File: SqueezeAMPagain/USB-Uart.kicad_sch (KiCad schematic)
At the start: 12 parts, among them J5 USB_B_Micro, J9 Conn_01x06_Pin, Q4 Q_NPN_BEC, Q5 Q_NPN_BEC, U3 CP2102N-Axx-xQFN28

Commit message: Update SqueezeAMPagain.kicad_pcb, SqueezeAMPagain.kicad_prl, USB-Uart.kicad_sch, and 4 more files
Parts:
- removed L10: 680nH, Inductor_SMD:L_0805_2012Metric, symbol Device:L
- added C76, C77, C80: 100n, Capacitor_SMD:C_0603_1608Metric, symbol Device:C
- added C78, C79: 2.2u/25V, Capacitor_SMD:C_0805_2012Metric, symbol Device:C
- added FB6: 600Ω@100MHz 500mA, Inductor_SMD:L_0805_2012Metric, symbol Device:FerriteBead_Small
- added R29, R30, R31: 10k, Resistor_SMD:R_0603_1608Metric, symbol Device:R
- added U7: AMS1117-3.3, Package_TO_SOT_SMD:SOT-223-3_TabPin2, symbol Regulator_Linear:AMS1117-3.3
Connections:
- net +3.3V: now also C76.1, U7.2 (VO)
- net GND: now also C76.2, C77.2, C78.2, R31.1, U7.1 (GND)
- net V_{USB}: now also U3.7 (VREGIN), C77.1, C78.1, FB6.2, R29.1, R30.1, U7.3 (VI); no longer U3.8 (VBUS)
- net at D1.1 (K): now also FB6.1
- net at U3.6 (VDD): now also C79.1, C80.1
- new net: R29.2, R30.2, R31.2, U3.8 (VBUS)
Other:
- note added: "max Output of internal regulator?"
- moved on the sheet: C46, C47

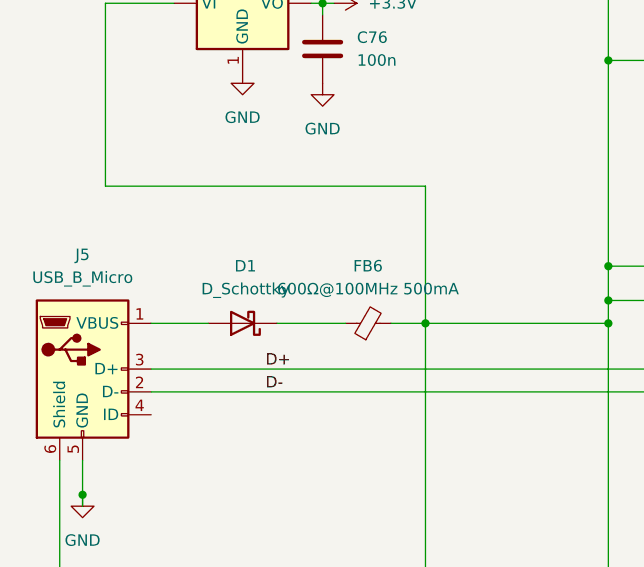
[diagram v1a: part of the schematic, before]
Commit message: Update SqueezeAMPagain.kicad_pcb, SqueezeAMPagain.kicad_sch, USB-Uart.kicad_sch, and 4 more files
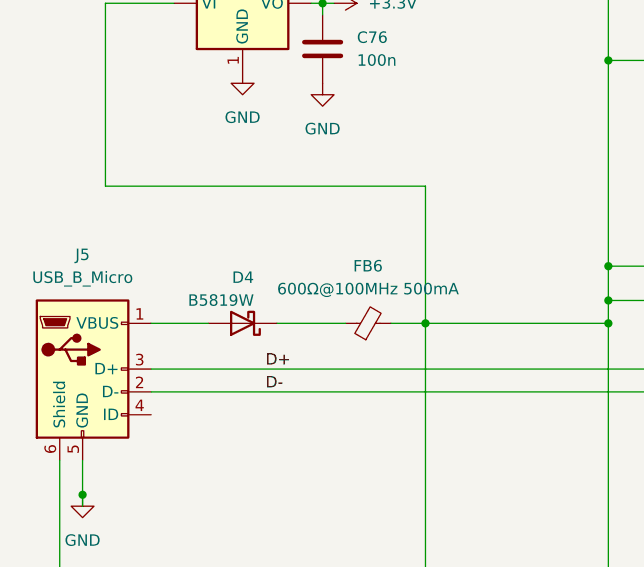
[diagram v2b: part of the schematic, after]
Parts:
- removed D1: D_Schottky, Diode_SMD:D_0603_1608Metric, symbol Device:D_Schottky
- added D4: B5819W, Diode_SMD:D_SOD-123, symbol Device:D_Schottky
- R29, R30, R31: JLCPCB# (none) -> C25804
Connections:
- net at FB6.1: now also D4.1 (K)
- net at J5.1 (VBUS): now also D4.2 (A)
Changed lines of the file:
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@@
+	)
+	(symbol
+		(lib_id "Device:C")
+		(at 80.01 116.84 0)
+		(unit 1)
+		(exclude_from_sim no)
+		(in_bom yes)
+		(on_board yes)
+		(dnp no)
+		(fields_autoplaced yes)
+		(property "Reference" "C47"
+			(at 83.82 115.5699 0)
+			(effects
+				(font
+					(size 1.27 1.27)
+				)
+				(justify left)
+			)
+		)
+		(property "Value" "2.2u/25V"
+			(at 83.82 118.1099 0)
+			(effects
+				(font
+					(size 1.27 1.27)
+				)
+				(justify left)
+			)
+		)
+		(property "Footprint" "Capacitor_SMD:C_0805_2012Metric"
+			(at 80.9752 120.65 0)
+			(effects
+				(font
+					(size 1.27 1.27)
+				)
+				(hide yes)
+			)
+		)
+		(property "Datasheet" "~"
+			(at 80.01 116.84 0)
+			(effects
+				(font
+					(size 1.27 1.27)
+				)
+				(hide yes)
+			)
+		)
+		(property "Description" "Unpolarized capacitor"
+			(at 80.01 116.84 0)
+			(effects
+				(font
+					(size 1.27 1.27)
+				)
+				(hide yes)
+			)
+		)
+		(pin "2"
+		)
+		(pin "1"
+		)
+		(instances
+			(project "SqueezeAMPagain"
+				(path "/3675160b-d9e5-490e-b506-2a7966e79ed0/86167bdd-1d24-4489-95f0-02f70a80611f"
+					(reference "C47")
+					(unit 1)
+				)
+			)
+		)
+	)
+	(symbol
+		(lib_id "Device:Q_NPN_BEC")
+		(at 189.23 85.09 0)
+		(unit 1)
+		(exclude_from_sim no)
+		(in_bom yes)
+		(on_board yes)
+		(dnp no)
+		(fields_autoplaced yes)
+		(property "Reference" "Q4"
+			(at 194.31 83.8199 0)
+			(effects
+				(font
+					(size 1.27 1.27)
+				)
+				(justify left)
+			)
+		)
+		(property "Value" "Q_NPN_BEC"
+			(at 194.31 86.3599 0)
+			(effects
+				(font
+					(size 1.27 1.27)
+				)
+				(justify left)
+			)
+		)
+		(property "Footprint" "Package_TO_SOT_SMD:SOT-23"
+			(at 194.31 82.55 0)
+			(effects
+				(font
+					(size 1.27 1.27)
+				)
+				(hide yes)
+			)
+		)
+		(property "Datasheet" "~"
+			(at 189.23 85.09 0)
+			(effects
+				(font
+					(size 1.27 1.27)
+				)
+				(hide yes)
+			)
+		)
+		(property "Description" "NPN transistor, base/emitter/collector"
+			(at 189.23 85.09 0)
+			(effects
+				(font
+					(size 1.27 1.27)
+				)
+				(hide yes)
+			)
+		)
+		(pin "3"
+		)
+		(pin "2"
+		)
+		(pin "1"
+		)
+		(instances
+			(project "SqueezeAMPagain"
+				(path "/3675160b-d9e5-490e-b506-2a7966e79ed0/86167bdd-1d24-4489-95f0-02f70a80611f"
+					(reference "Q4")
+					(unit 1)
+				)
+			)
+		)
 	)
 	(symbol
@@
 		(on_board yes)
 		(dnp no)
-		(fields_autoplaced yes)
-		(property "Reference" "D1"
-			(at 39.6875 62.23 0)
-			(effects
-				(font
-					(size 1.27 1.27)
-				)
-			)
-		)
-		(property "Value" "D_Schottky"
-			(at 39.6875 64.77 0)
-			(effects
-				(font
-					(size 1.27 1.27)
-				)
-			)
-		)
-		(property "Footprint" "Diode_SMD:D_0603_1608Metric"
+		(property "Reference" "D4"
+			(at 40.64 63.5 0)
+			(effects
+				(font
+					(size 1.27 1.27)
+				)
+				(justify left)
+			)
+		)
+		(property "Value" "B5819W"
+			(at 40.64 66.04 0)
+			(effects
+				(font
+					(size 1.27 1.27)
+				)
+				(justify left)
+			)
+		)
+		(property "Footprint" "Diode_SMD:D_SOD-123"
 			(at 39.37 68.58 0)
 			(effects
@@
 			)
 		)
+		(property "JLCPCB#" "C8598"
+			(at 39.37 68.58 90)
+			(effects
+				(font
+					(size 1.27 1.27)
+				)
+				(hide yes)
+			)
+		)
+		(pin "1"
+		)
 		(pin "2"
 		)
-		(pin "1"
-		)
-		(instances
-			(project ""
-				(path "/3675160b-d9e5-490e-b506-2a7966e79ed0/86167bdd-1d24-4489-95f0-02f70a80611f"
-					(reference "D1")
-					(unit 1)
-				)
-			)
-		)
-	)
-	(symbol
-		(lib_id "Device:C")
-		(at 80.01 116.84 0)
-		(unit 1)
-		(exclude_from_sim no)
-		(in_bom yes)
-		(on_board yes)
-		(dnp no)
-		(fields_autoplaced yes)
-		(property "Reference" "C47"
-			(at 83.82 115.5699 0)
-			(effects
-				(font
-					(size 1.27 1.27)
-				)
-				(justify left)
-			)
-		)
-		(property "Value" "2.2u/25V"
-			(at 83.82 118.1099 0)
-			(effects
-				(font
-					(size 1.27 1.27)
-				)
-				(justify left)
-			)
-		)
-		(property "Footprint" "Capacitor_SMD:C_0805_2012Metric"
-			(at 80.9752 120.65 0)
-			(effects
-				(font
-					(size 1.27 1.27)
-				)
-				(hide yes)
-			)
-		)
-		(property "Datasheet" "~"
-			(at 80.01 116.84 0)
-			(effects
-				(font
-					(size 1.27 1.27)
-				)
-				(hide yes)
-			)
-		)
-		(property "Description" "Unpolarized capacitor"
-			(at 80.01 116.84 0)
-			(effects
-				(font
-					(size 1.27 1.27)
-				)
-				(hide yes)
-			)
-		)
-		(pin "2"
-		)
-		(pin "1"
-		)
-		(instances
-			(project "SqueezeAMPagain"
-				(path "/3675160b-d9e5-490e-b506-2a7966e79ed0/86167bdd-1d24-4489-95f0-02f70a80611f"
-					(reference "C47")
-					(unit 1)
-				)
-			)
-		)
-	)
-	(symbol
-		(lib_id "Device:Q_NPN_BEC")
-		(at 189.23 85.09 0)
-		(unit 1)
-		(exclude_from_sim no)
-		(in_bom yes)
-		(on_board yes)
-		(dnp no)
-		(fields_autoplaced yes)
-		(property "Reference" "Q4"
-			(at 194.31 83.8199 0)
-			(effects
-				(font
-					(size 1.27 1.27)
-				)
-				(justify left)
-			)
-		)
-		(property "Value" "Q_NPN_BEC"
-			(at 194.31 86.3599 0)
-			(effects
-				(font
-					(size 1.27 1.27)
-				)
-				(justify left)
-			)
-		)
-		(property "Footprint" "Package_TO_SOT_SMD:SOT-23"
-			(at 194.31 82.55 0)
-			(effects
-				(font
-					(size 1.27 1.27)
-				)
-				(hide yes)
-			)
-		)
-		(property "Datasheet" "~"
-			(at 189.23 85.09 0)
-			(effects
-				(font
-					(size 1.27 1.27)
-				)
-				(hide yes)
-			)
-		)
-		(property "Description" "NPN transistor, base/emitter/collector"
-			(at 189.23 85.09 0)
-			(effects
-				(font
-					(size 1.27 1.27)
-				)
-				(hide yes)
-			)
-		)
-		(pin "3"
-		)
-		(pin "2"
-		)
-		(pin "1"
-		)
-		(instances
-			(project "SqueezeAMPagain"
-				(path "/3675160b-d9e5-490e-b506-2a7966e79ed0/86167bdd-1d24-4489-95f0-02f70a80611f"
-					(reference "Q4")
+		(instances
+			(project "SqueezeAMPagain"
+				(path "/3675160b-d9e5-490e-b506-2a7966e79ed0/86167bdd-1d24-4489-95f0-02f70a80611f"
+					(reference "D4")
 					(unit 1)
 				)
@@
 			)
 		)
+		(property "JLCPCB#" "C25804"
+			(at 90.17 62.23 0)
+			(effects
+				(font
+					(size 1.27 1.27)
+				)
+				(hide yes)
+			)
+		)
 		(pin "1"
 		)
@@
 		)
 		(property "Description" "Resistor"
+			(at 90.17 66.04 0)
+			(effects
+				(font
+					(size 1.27 1.27)
+				)
+				(hide yes)
+			)
+		)
+		(property "JLCPCB#" "C25804"
 			(at 90.17 66.04 0)
 			(effects
@@
 			(at 101.6 87.63 0)
 			(effects
+				(font
+					(size 1.27 1.27)
+				)
+				(hide yes)
+			)
+		)
+		(property "JLCPCB#" "C25804"
+			(at 101.6 87.63 0)
+			(effects

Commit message: Update SqueezeAMPagain.kicad_pcb, SqueezeAMPagain.kicad_prl, SqueezeAMPagain.kicad_pro, and 6 more files
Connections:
- net GND: now also C79.2, C80.2
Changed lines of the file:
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@@
+	)
+	(symbol
+		(lib_id "power:GND")
+		(at 134.62 49.53 0)
+		(unit 1)
+		(exclude_from_sim no)
+		(in_bom yes)
+		(on_board yes)
+		(dnp no)
+		(fields_autoplaced yes)
+		(property "Reference" "#PWR0109"
+			(at 134.62 55.88 0)
+			(effects
+				(font
+					(size 1.27 1.27)
+				)
+				(hide yes)
+			)
+		)
+		(property "Value" "GND"
+			(at 134.62 54.61 0)
+			(effects
+				(font
+					(size 1.27 1.27)
+				)
+			)
+		)
+		(property "Footprint" ""
+			(at 134.62 49.53 0)
+			(effects
+				(font
+					(size 1.27 1.27)
+				)
+				(hide yes)
+			)
+		)
+		(property "Datasheet" ""
+			(at 134.62 49.53 0)
+			(effects
+				(font
+					(size 1.27 1.27)
+				)
+				(hide yes)
+			)
+		)
+		(property "Description" "Power symbol creates a global label with name \"GND\" , ground"
+			(at 134.62 49.53 0)
+			(effects
+				(font
+					(size 1.27 1.27)
+				)
+				(hide yes)
+			)
+		)
+		(pin "1"
+		)
+		(instances
+			(project "SqueezeAMPagain"
+				(path "/3675160b-d9e5-490e-b506-2a7966e79ed0/86167bdd-1d24-4489-95f0-02f70a80611f"
+					(reference "#PWR0109")
+					(unit 1)
+				)
+			)
+		)
 	)
 	(symbol
@@
 					(unit 1)
 				)
+			)
+		)
+	)
+	(symbol
+		(lib_id "power:GND")
+		(at 147.32 49.53 0)
+		(unit 1)
+		(exclude_from_sim no)
+		(in_bom yes)
+		(on_board yes)
+		(dnp no)
+		(fields_autoplaced yes)
+		(property "Reference" "#PWR0110"
+			(at 147.32 55.88 0)
+			(effects
+				(font
+					(size 1.27 1.27)
+				)
+				(hide yes)
+			)
+		)
+		(property "Value" "GND"
+			(at 147.32 54.61 0)
+			(effects
+				(font
+					(size 1.27 1.27)
+				)
+			)
+		)
+		(property "Footprint" ""
+			(at 147.32 49.53 0)
+			(effects
+				(font
+					(size 1.27 1.27)
+				)
+				(hide yes)
+			)
+		)
+		(property "Datasheet" ""
+			(at 147.32 49.53 0)
+			(effects
+				(font
+					(size 1.27 1.27)
+				)
+				(hide yes)
+			)
+		)
+		(property "Description" "Power symbol creates a global label with name \"GND\" , ground"
+			(at 147.32 49.53 0)
+			(effects
+				(font
+					(size 1.27 1.27)
+				)
+				(hide yes)
+			)
+		)
+		(pin "1"
+		)
+		(instances
+			(project "SqueezeAMPagain"
+				(path "/3675160b-d9e5-490e-b506-2a7966e79ed0/86167bdd-1d24-4489-95f0-02f70a80611f"
+					(reference "#PWR0110")
+					(unit 1)
+				)

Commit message: Update SqueezeAMPagain.kicad_pcb, SqueezeAMPagain.kicad_prl, SqueezeAMPagain.kicad_pro, and 7 more files
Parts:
- removed C76: 100n, Capacitor_SMD:C_0603_1608Metric, symbol Device:C
- removed U7: AMS1117-3.3, Package_TO_SOT_SMD:SOT-223-3_TabPin2, symbol Regulator_Linear:AMS1117-3.3

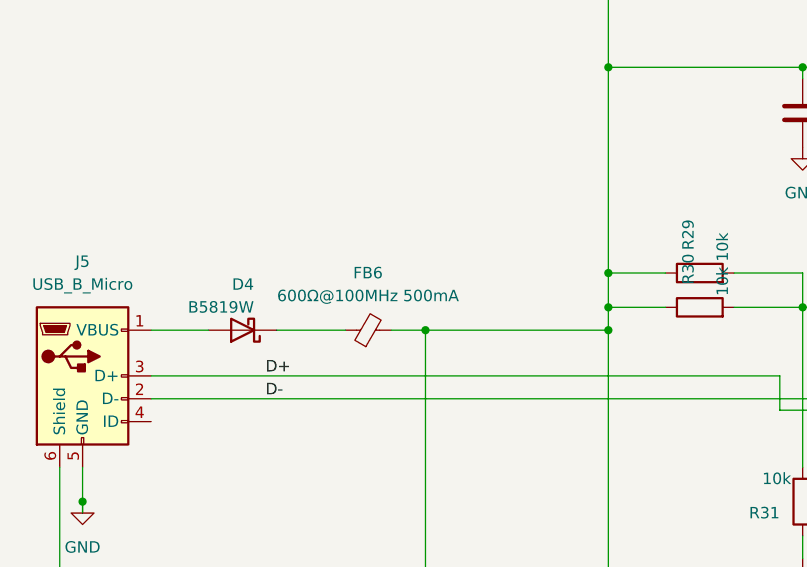
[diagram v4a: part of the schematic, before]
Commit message: Update SqueezeAMPagain.kicad_pcb, SqueezeAMPagain.kicad_prl, SqueezeAMPagain.kicad_pro, and 5 more files
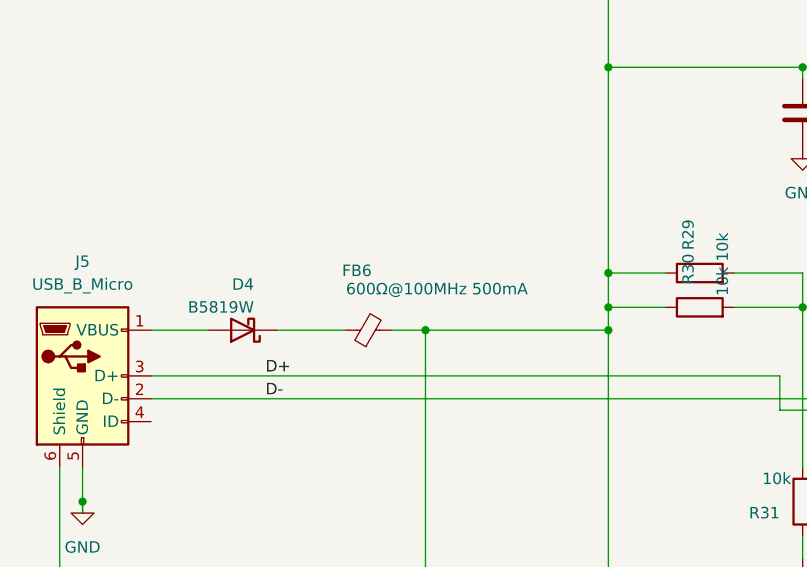
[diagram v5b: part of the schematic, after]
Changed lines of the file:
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@@
+		)
+	)
+	(netclass_flag ""
+		(length 2.54)
+		(shape round)
+		(at 33.02 73.66 0)
+		(fields_autoplaced yes)
+		(effects
+			(font
+				(size 1.27 1.27)
+			)
+			(justify left bottom)
+		)
+		(property "Netclass" "USB"
+			(at 33.7185 71.12 0)
+			(effects
+				(font
+					(size 1.27 1.27)
+					(italic yes)
+				)
+				(justify left)
+			)
+		)
+	)
+	(netclass_flag ""
+		(length 2.54)
+		(shape round)
+		(at 46.99 68.58 0)
+		(effects
+			(font
+				(size 1.27 1.27)
+			)
+			(justify left bottom)
+		)
+		(property "Netclass" "Supply"
+			(at 46.736 65.278 90)
+			(effects
+				(font
+					(size 1.27 1.27)
+					(italic yes)
+				)
+				(justify left)
+			)
+		)
+	)
+	(netclass_flag ""
+		(length 2.54)
+		(shape round)
+		(at 68.58 68.58 0)
+		(fields_autoplaced yes)
+		(effects
+			(font
+				(size 1.27 1.27)
+			)
+			(justify left bottom)
+		)
+		(property "Netclass" "Supply"
+			(at 69.2785 66.04 0)
+			(effects
+				(font
+					(size 1.27 1.27)
+					(italic yes)
+				)
+				(justify left)
+			)
+		)
+	)
+	(netclass_flag ""
+		(length 2.54)
+		(shape round)
+		(at 33.02 76.2 180)
+		(fields_autoplaced yes)
+		(effects
+			(font
+				(size 1.27 1.27)
+			)
+			(justify right bottom)
+		)
+		(property "Netclass" "USB"
+			(at 33.7185 78.74 0)
+			(effects
+				(font
+					(size 1.27 1.27)
+					(italic yes)
+				)
+				(justify left)
+			)
+		)
+	)
+	(netclass_flag ""
+		(length 2.54)
+		(shape round)
+		(at 30.48 68.58 0)
+		(effects
+			(font
+				(size 1.27 1.27)
+			)
+			(justify left bottom)
+		)
+		(property "Netclass" "Supply"
+			(at 30.226 65.278 90)
+			(effects
+				(font
+					(size 1.27 1.27)
+					(italic yes)
+				)
+				(justify left)
+			)
 		)
 	)
@@
 		(on_board yes)
 		(dnp no)
-		(fields_autoplaced yes)
 		(property "Reference" "FB6"
-			(at 53.3019 62.23 90)
+			(at 52.07 61.976 90)
 			(effects
 				(font
@@
 		)
 		(property "Value" "600Ω@100MHz 500mA"
-			(at 53.3019 64.77 90)
-			(effects
-				(font
+			(at 60.96 64.008 90)
+			(effects
+				(font

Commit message: Update SqueezeAMPagain.kicad_pcb, SqueezeAMPagain.kicad_prl, SqueezeAMPagain.kicad_pro, and 11 more files
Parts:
- J8: renamed from J5; footprint Connector_USB:USB_Micro-B_Wuerth_629105150521_CircularHoles -> Connector_USB:USB_Micro-B_XKB_U254-051T-4BH83-F1S
- renumbered C48 to C83, C46 to C84, C47 to C85, C78 to C86, C77 to C87, C80 to C88, C79 to C89, D4 to D3, Q4 to Q8, Q5 to Q9, R29 to R35, R30 to R36, R31 to R37, R6 to R38, R7 to R39, U3 to U7

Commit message: Update SqueezeAMPagain.kicad_pcb, SqueezeAMPagain.kicad_prl, SqueezeAMPagain.kicad_pro, and 7 more files
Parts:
- J8: footprint Connector_USB:USB_Micro-B_XKB_U254-051T-4BH83-F1S -> usb_micro_xnj073:usb_micro_xnj_073
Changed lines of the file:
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@@
 			)
 		)
-		(property "Footprint" "Connector_USB:USB_Micro-B_XKB_U254-051T-4BH83-F1S"
+		(property "Footprint" "usb_micro_xnj073:usb_micro_xnj_073"
 			(at 25.4 74.93 0)
 			(effects

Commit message: Update SqueezeAMPagain.kicad_pcb, SqueezeAMPagain.kicad_prl, SqueezeAMPagain.kicad_pro, and 11 more files
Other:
- title: (none) -> SqueezeAMP_{again}
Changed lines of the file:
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@@
 	(generator_version "8.0")
 	(paper "A4")
+	(title_block
+		(title "SqueezeAMP_{again}")
+		(date "2024-08-23")
+		(rev "1.0")
+	)
 	(junction
 		(at 168.91 72.39)
